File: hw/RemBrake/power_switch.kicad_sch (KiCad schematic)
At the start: 53 parts, among them Q1 SiS415DNT, Q2 BC337, Q3 BC847, Q4 BC337, Q5 BC847, Q6 BC337, Q7 BC847, U1 TPS62140, U2 BD5230G-TR, U3 XC6220B331MR, U4 MAX40200AUK

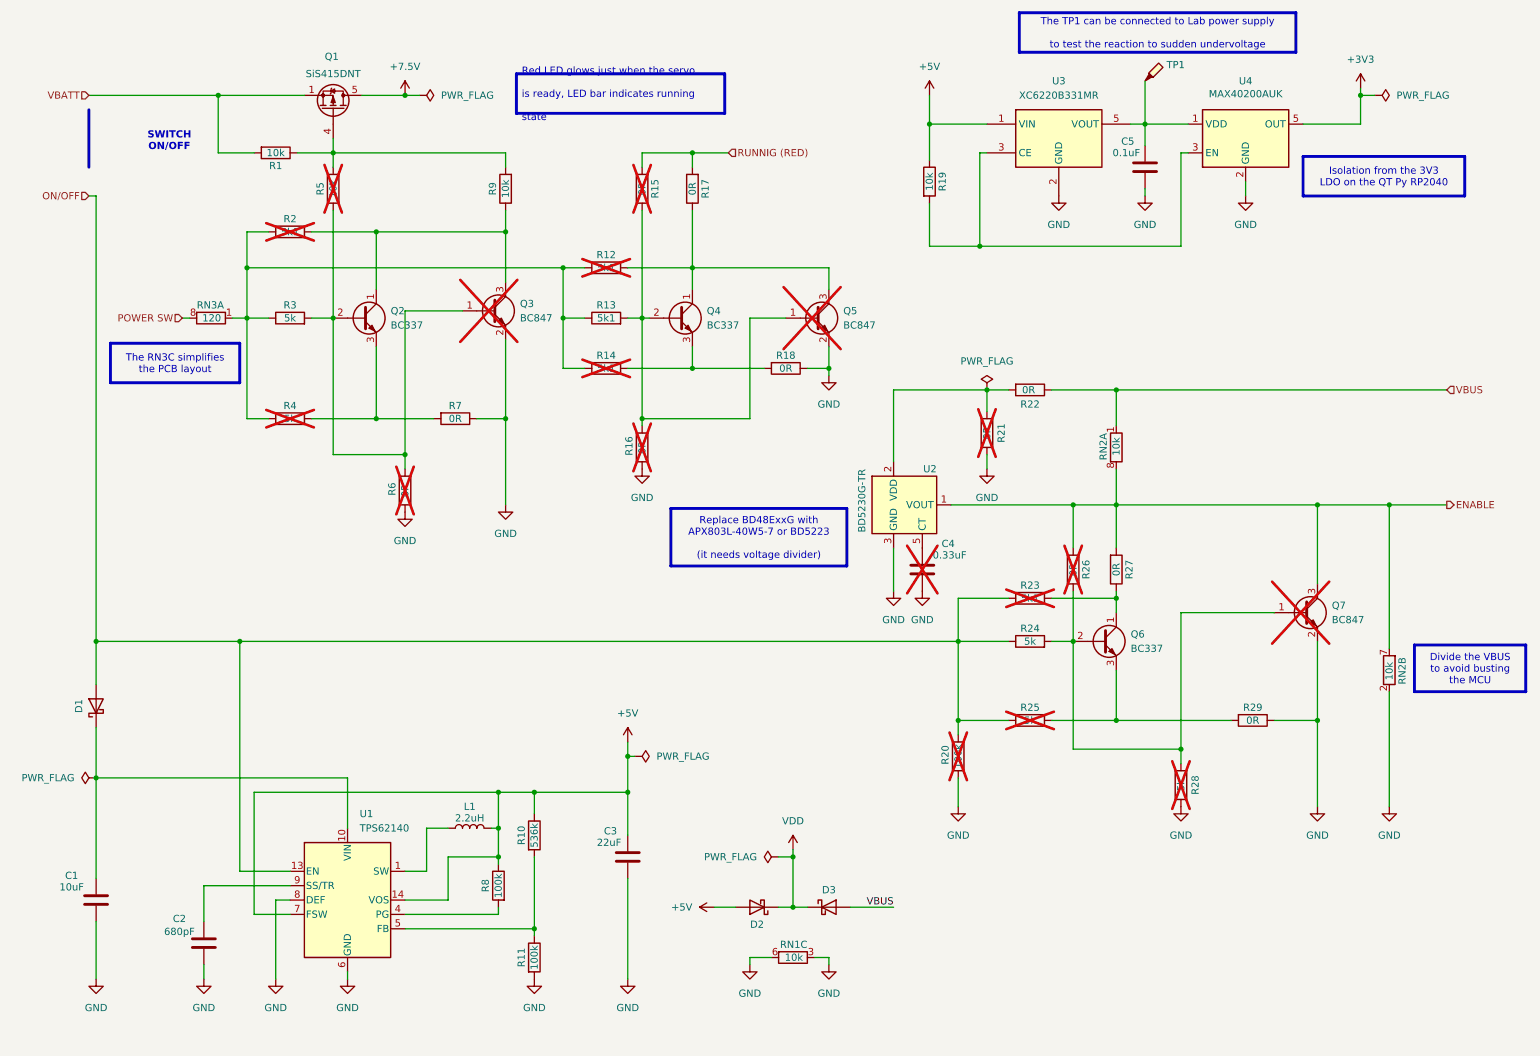
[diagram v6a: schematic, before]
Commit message: added resistor for the ideal diode enable and new annotation
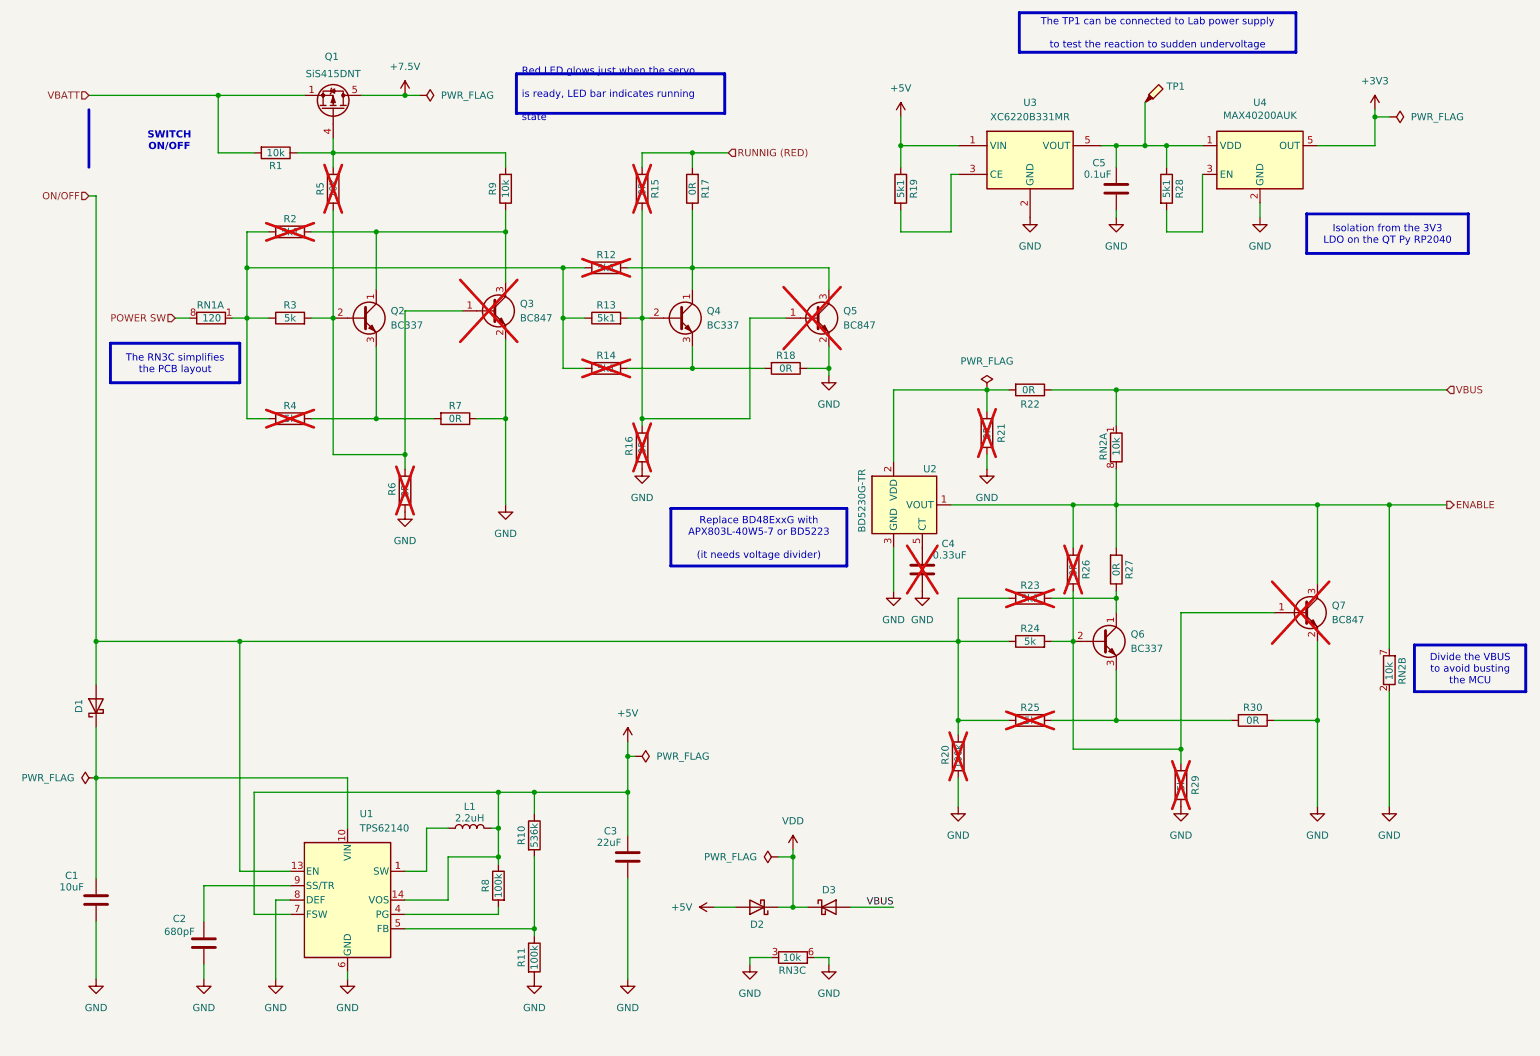
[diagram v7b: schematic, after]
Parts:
- removed RN1: 10k, Resistor_SMD:R_Array_Convex_4x0603, symbol Device:R_Pack04_Split
- added R28: 5k1, Resistor_SMD:R_0805_2012Metric_Pad1.20x1.40mm_HandSolder, symbol Device:R
- added RN3: 10k, Resistor_SMD:R_Array_Convex_4x0603, symbol Device:R_Pack04_Split
- R19: value 10k -> 5k1
- renumbered R28 to R29, R29 to R30, RN3 to RN1
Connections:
- net GND: now also RN3.3 (R3.1), RN3.6 (R3.2)
- net at R19.2, U3.3 (CE): no longer U4.3 (EN)
- net at C5.1, TP1.1, U3.5 (VOUT)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: now also R28.1
- new net: R28.2, U4.3 (EN)
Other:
- moved on the sheet: C5, R19, TP1, U3, U4

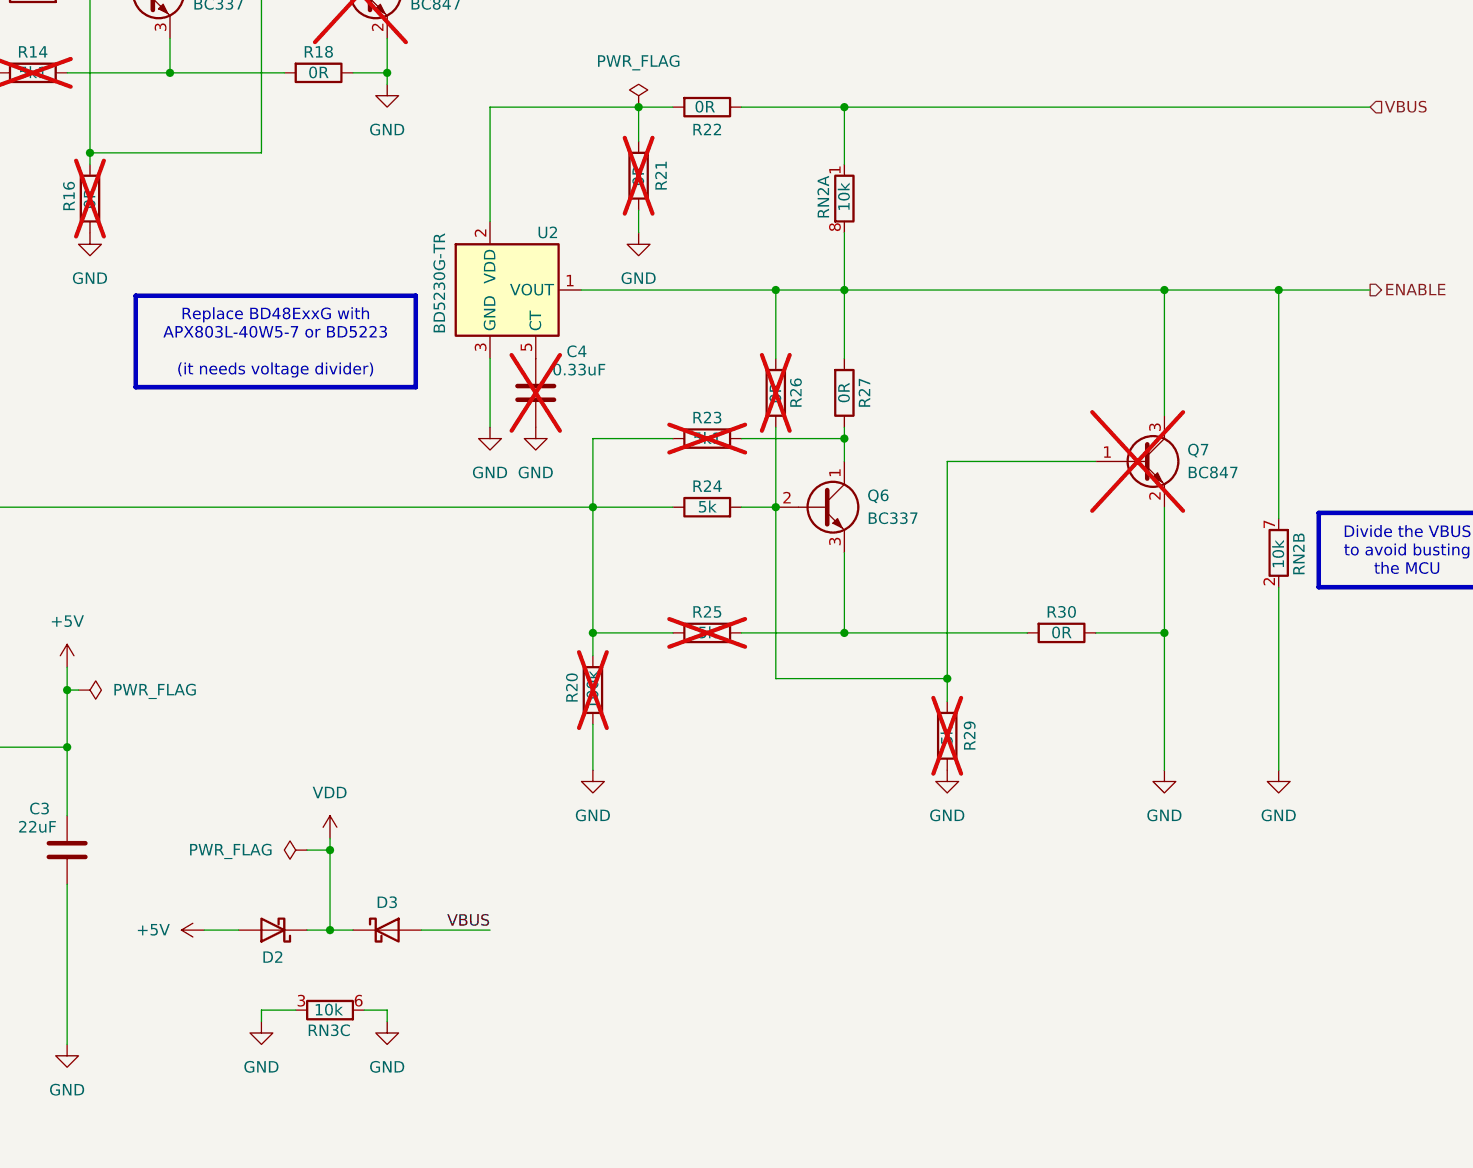
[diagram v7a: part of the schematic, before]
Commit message: finished new version of pcb with transistors gating vbus and fixed ledbar functionality
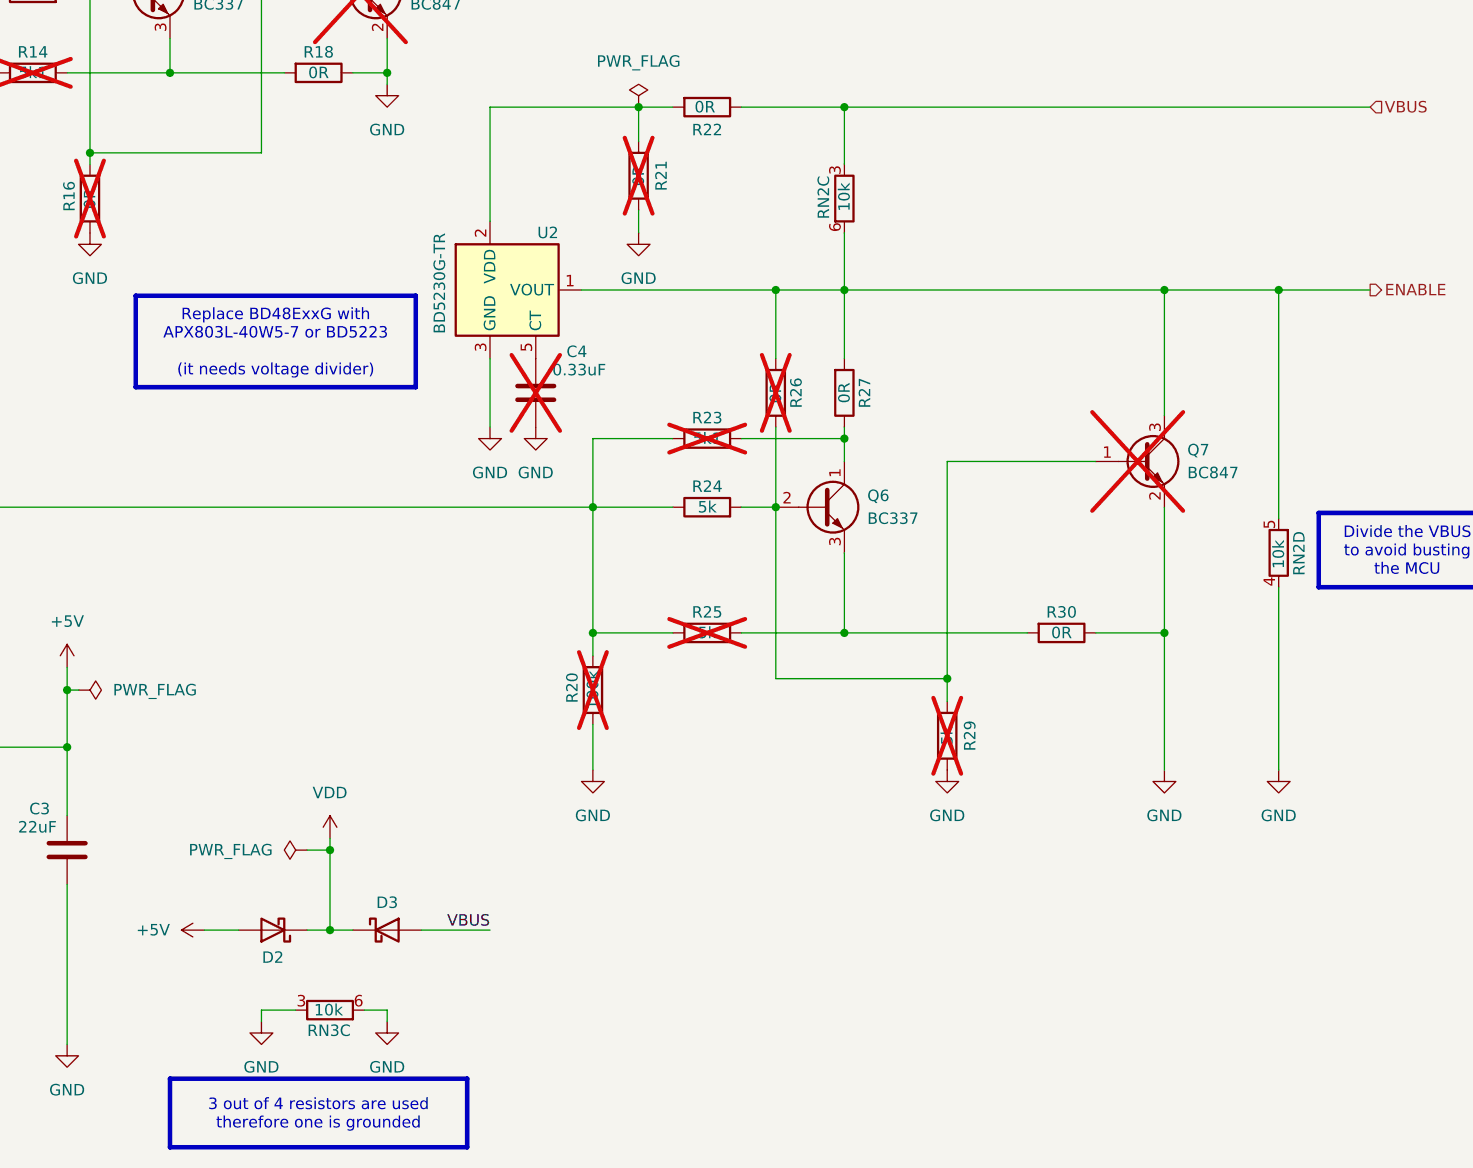
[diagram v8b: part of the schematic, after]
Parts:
- removed RN2: 10k, Resistor_SMD:R_Array_Convex_4x0603, symbol Device:R_Pack04_Split
- added RN2: 10k, Resistor_SMD:R_Array_Convex_4x0603, symbol Device:R_Pack04_Split
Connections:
- net ENABLE: now also RN2.5 (R4.2), RN2.6 (R3.2)
- net GND: now also RN2.4 (R4.1)
- net VBUS: now also RN2.3 (R3.1)
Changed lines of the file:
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@@
 		)
 	)
+	(text_box "3 out of 4 resistors are used\ntherefore one is grounded"
+		(exclude_from_sim no)
+		(at 134.62 187.96 0)
+		(size 33.02 7.62)
+		(margins 0.9525 0.9525 0.9525 0.9525)
+		(stroke
+			(width 0.508)
+			(type solid)
+			(color 128 63 0 1)
+		)
+		(fill
+			(type color)
+			(color 255 255 153 1)
+		)
+		(effects
+			(font
+				(size 1.27 1.27)
+			)
+		)
+	)
 	(junction
 		(at 71.12 67.31)
@@
 	)
 	(symbol
-		(lib_id "Device:R_Pack04_Split")
-		(at 257.81 129.54 0)
-		(unit 2)
-		(exclude_from_sim no)
-		(in_bom yes)
-		(on_board yes)
-		(dnp no)
-		(property "Reference" "RN2"
-			(at 260.096 132.08 90)
-			(effects
-				(font
-					(size 1.27 1.27)
-				)
-				(justify left)
-			)
-		)
-		(property "Value" "10k"
-			(at 257.81 131.318 90)
-			(effects
-				(font
-					(size 1.27 1.27)
-				)
-				(justify left)
-			)
-		)
-		(property "Footprint" "Resistor_SMD:R_Array_Convex_4x0603"
-			(at 255.778 129.54 90)
-			(hide yes)
-			(effects
-				(font
-					(size 1.27 1.27)
-				)
-			)
-		)
-		(property "Datasheet" ""
-			(at 257.81 129.54 0)
-			(hide yes)
-			(effects
-				(font
-					(size 1.27 1.27)
-				)
-			)
-		)
-		(property "Description" "4 resistor network, parallel topology, split"
-			(at 257.81 129.54 0)
-			(hide yes)
-			(effects
-				(font
-					(size 1.27 1.27)
-				)
-			)
-		)
-		(pin "5"
-		)
-		(pin "8"
-		)
-		(pin "2"
-		)
-		(pin "1"
-		)
-		(pin "6"
-		)
-		(pin "3"
-		)
-		(pin "4"
-		)
-		(pin "7"
-		)
-		(instances
-			(project "RemBrake"
-				(path "/e6d4ae5b-c9d7-4cbe-b288-c929fdf55a75/2d0cc746-3115-4ebf-adba-86e7fd6ac8bd"
-					(reference "RN2")
-					(unit 2)
-				)
-			)
-		)
-	)
-	(symbol
 		(lib_id "Device:R")
 		(at 119.38 58.42 90)
@@
 	)
 	(symbol
+		(lib_id "Device:R_Pack04_Split")
+		(at 257.81 129.54 0)
+		(unit 4)
+		(exclude_from_sim no)
+		(in_bom yes)
+		(on_board yes)
+		(dnp no)
+		(property "Reference" "RN2"
+			(at 260.096 132.08 90)
+			(effects
+				(font
+					(size 1.27 1.27)
+				)
+				(justify left)
+			)
+		)
+		(property "Value" "10k"
+			(at 257.81 131.318 90)
+			(effects
+				(font
+					(size 1.27 1.27)
+				)
+				(justify left)
+			)
+		)
+		(property "Footprint" "Resistor_SMD:R_Array_Convex_4x0603"
+			(at 255.778 129.54 90)
+			(hide yes)
+			(effects
+				(font
+					(size 1.27 1.27)
+				)
+			)
+		)
+		(property "Datasheet" ""
+			(at 257.81 129.54 0)
+			(hide yes)
+			(effects
+				(font
+					(size 1.27 1.27)
+				)
+			)
+		)
+		(property "Description" "4 resistor network, parallel topology, split"
+			(at 257.81 129.54 0)
+			(hide yes)
+			(effects
+				(font
+					(size 1.27 1.27)
+				)
+			)
+		)
+		(pin "5"
+		)
+		(pin "8"
+		)
+		(pin "2"
+		)
+		(pin "1"
+		)
+		(pin "6"
+		)
+		(pin "3"
+		)
+		(pin "4"
+		)
+		(pin "7"
+		)
+		(instances
+			(project "RemBrake"
+				(path "/e6d4ae5b-c9d7-4cbe-b288-c929fdf55a75/2d0cc746-3115-4ebf-adba-86e7fd6ac8bd"
+					(reference "RN2")
+					(unit 4)
+				)
+			)
+		)
+	)
+	(symbol
 		(lib_id "Device:R")
 		(at 233.68 138.43 270)
@@
 	)
 	(symbol
+		(lib_id "Device:R_Pack04_Split")
+		(at 209.55 90.17 180)
+		(unit 3)
+		(exclude_from_sim no)
+		(in_bom yes)
+		(on_board yes)
+		(dnp no)
+		(property "Reference" "RN2"
+			(at 207.264 87.63 90)
+			(effects
+				(font
+					(size 1.27 1.27)
+				)
+				(justify left)
+			)
+		)
+		(property "Value" "10k"
+			(at 209.55 88.392 90)
+			(effects
+				(font
+					(size 1.27 1.27)
+				)
+				(justify left)
+			)
+		)
+		(property "Footprint" "Resistor_SMD:R_Array_Convex_4x0603"
+			(at 211.582 90.17 90)
+			(hide yes)
+			(effects
+				(font
+					(size 1.27 1.27)
+				)
+			)
+		)
+		(property "Datasheet" ""
+			(at 209.55 90.17 0)
+			(hide yes)
+			(effects
+				(font
+					(size 1.27 1.27)
+				)
+			)
+		)
+		(property "Description" "4 resistor network, parallel topology, split"
+			(at 209.55 90.17 0)
+			(hide yes)
+			(effects
+				(font
+					(size 1.27 1.27)
+				)
+			)
+		)
+		(pin "5"
+		)
+		(pin "8"
+		)
+		(pin "2"
+		)
+		(pin "1"
+		)
+		(pin "6"
+		)
+		(pin "3"
+		)
+		(pin "4"
+		)
+		(pin "7"
+		)
+		(instances
+			(project "RemBrake"
+				(path "/e6d4ae5b-c9d7-4cbe-b288-c929fdf55a75/2d0cc746-3115-4ebf-adba-86e7fd6ac8bd"
+					(reference "RN2")
+					(unit 3)
+				)
+			)
+		)
+	)
+	(symbol
 		(lib_id "power:PWR_FLAG")
 		(at 124.46 144.78 270)
@@
 					(unit 1)
 				)
-			)
-		)
-	)
-	(symbol
-		(lib_id "Device:R_Pack04_Split")
-		(at 209.55 90.17 180)
-		(unit 1)
-		(exclude_from_sim no)
-		(in_bom yes)
-		(on_board yes)
-		(dnp no)
-		(property "Reference" "RN2"
-			(at 207.264 87.63 90)
-			(effects
-				(font
-					(size 1.27 1.27)
-				)
-				(justify left)
-			)
-		)
-		(property "Value" "10k"
-			(at 209.55 88.392 90)
-			(effects
-				(font
-					(size 1.27 1.27)
-				)
-				(justify left)
-			)
-		)
-		(property "Footprint" "Resistor_SMD:R_Array_Convex_4x0603"
-			(at 211.582 90.17 90)
-			(hide yes)
-			(effects
-				(font
-					(size 1.27 1.27)
-				)
-			)
-		)
-		(property "Datasheet" ""
-			(at 209.55 90.17 0)
-			(hide yes)
-			(effects
-				(font
-					(size 1.27 1.27)
-				)
-			)
-		)
-		(property "Description" "4 resistor network, parallel topology, split"
-			(at 209.55 90.17 0)
-			(hide yes)
-			(effects
-				(font
-					(size 1.27 1.27)
-				)
-			)
-		)
-		(pin "5"
-		)
-		(pin "8"
-		)
-		(pin "2"
-		)
-		(pin "1"
-		)
-		(pin "6"
-		)
-		(pin "3"
-		)
-		(pin "4"
-		)
-		(pin "7"
-		)
-		(instances
-			(project "RemBrake"
-				(path "/e6d4ae5b-c9d7-4cbe-b288-c929fdf55a75/2d0cc746-3115-4ebf-adba-86e7fd6ac8bd"
-					(reference "RN2")
-					(unit 1)
-				)
